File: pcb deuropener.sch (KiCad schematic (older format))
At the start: 34 parts, among them J1 LED 1, J10 Duo LED, J11 Barrel_Jack_Switch, J12 RFID RC522, J13 Solenoid 12V, J14 jumper, J2 Button 2, J3 LED 2, J4 Button 1, J5 Buzzer 12V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

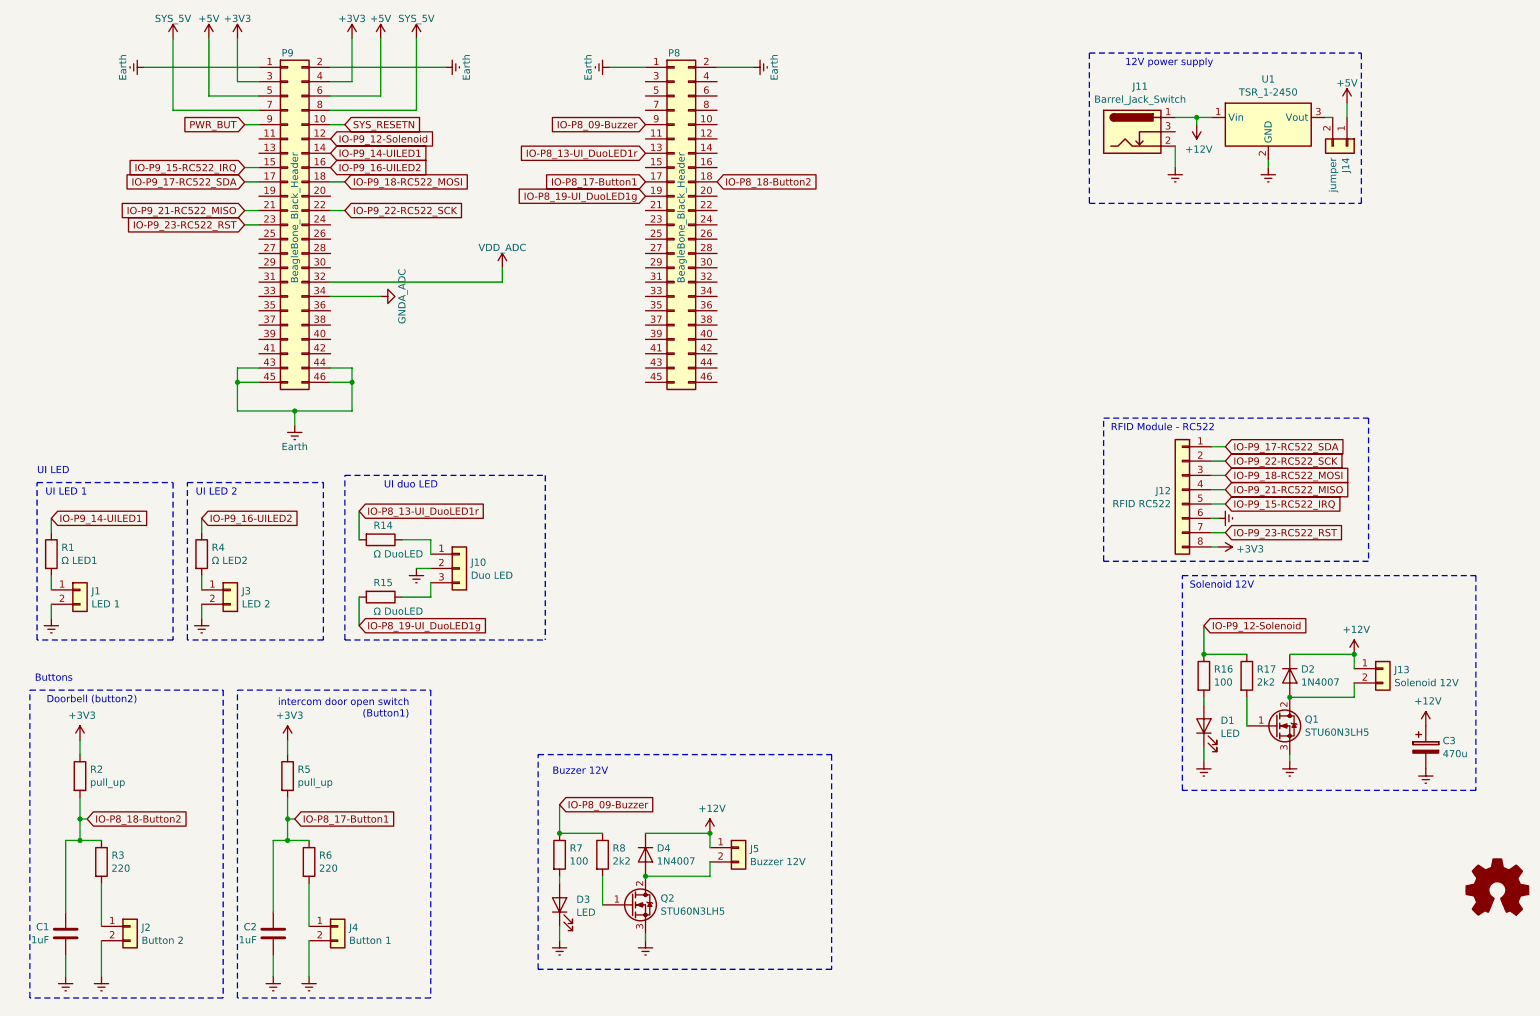
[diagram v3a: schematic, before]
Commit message: Remove a lot of parts and traces
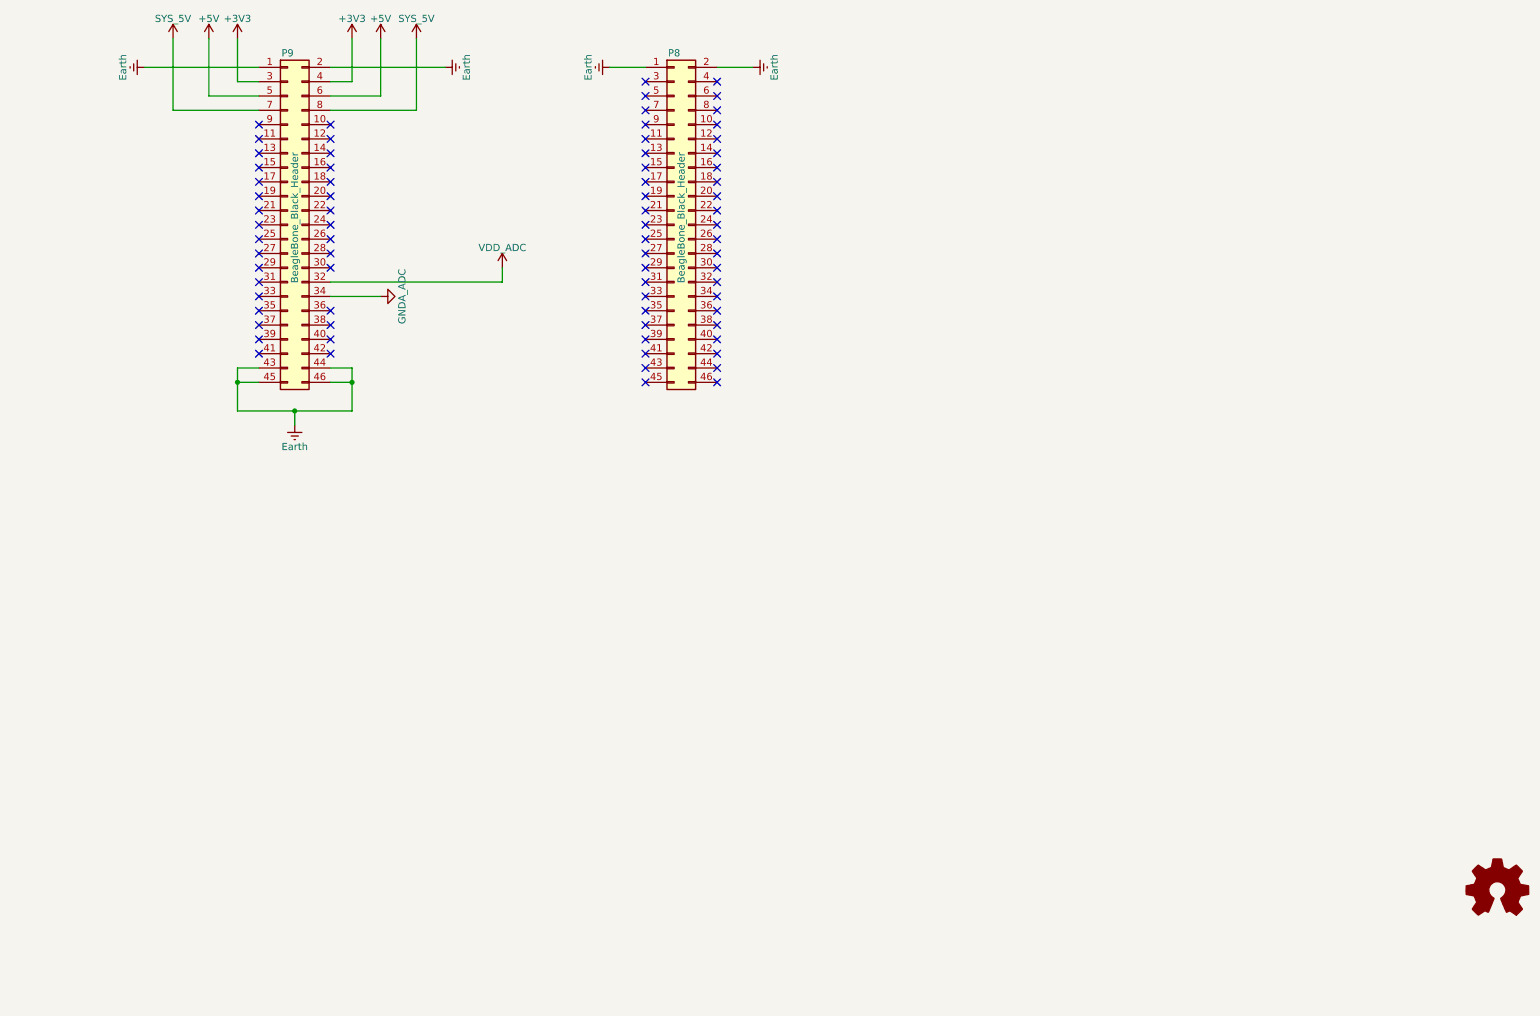
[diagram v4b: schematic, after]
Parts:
- removed C1, C2: 1uF, Capacitor_THT:C_Disc_D7.5mm_W4.4mm_P5.00mm, symbol Device:C
- removed C3: 470u, Capacitor_THT:CP_Radial_D10.0mm_P5.00mm, symbol Device:CP
- removed D1, D3: LED, LED_THT:LED_D5.0mm, symbol Device:LED
- removed D2, D4: 1N4007, Diode_THT:D_DO-41_SOD81_P10.16mm_Horizontal, symbol Diode:1N4007
- removed J1: LED 1, Connector_PinHeader_2.54mm:PinHeader_1x02_P2.54mm_Vertical, symbol Connector_Generic:Conn_01x02
- removed J10: Duo LED, Connector_PinHeader_2.54mm:PinHeader_1x03_P2.54mm_Vertical, symbol Connector_Generic:Conn_01x03
- removed J11: Barrel_Jack_Switch, Connector_BarrelJack:BarrelJack_Horizontal, symbol Connector:Barrel_Jack_Switch
- removed J12: RFID RC522, Connector_PinHeader_2.54mm:PinHeader_1x08_P2.54mm_Vertical, symbol Connector_Generic:Conn_01x08
- removed J13: Solenoid 12V, Connector_PinHeader_2.54mm:PinHeader_1x02_P2.54mm_Vertical, symbol Connector_Generic:Conn_01x02
- removed J14: jumper, Connector_PinHeader_2.54mm:PinHeader_1x02_P2.54mm_Vertical, symbol Connector_Generic:Conn_01x02
- removed J2: Button 2, Connector_PinHeader_2.54mm:PinHeader_1x02_P2.54mm_Vertical, symbol Connector_Generic:Conn_01x02
- removed J3: LED 2, Connector_PinHeader_2.54mm:PinHeader_1x02_P2.54mm_Vertical, symbol Connector_Generic:Conn_01x02
- removed J4: Button 1, Connector_PinHeader_2.54mm:PinHeader_1x02_P2.54mm_Vertical, symbol Connector_Generic:Conn_01x02
- removed J5: Buzzer 12V, Connector_PinHeader_2.54mm:PinHeader_1x02_P2.54mm_Vertical, symbol Connector_Generic:Conn_01x02
- removed Q1, Q2: STU60N3LH5, Package_TO_SOT_THT:SIPAK_Vertical, symbol Device:Q_NMOS_GDS
- removed R1: Ω LED1, Resistor_THT:R_Axial_DIN0207_L6.3mm_D2.5mm_P10.16mm_Horizontal, symbol Device:R
- removed R14, R15: Ω DuoLED, Resistor_THT:R_Axial_DIN0207_L6.3mm_D2.5mm_P10.16mm_Horizontal, symbol Device:R
- removed R16, R7: 100, Resistor_THT:R_Axial_DIN0207_L6.3mm_D2.5mm_P10.16mm_Horizontal, symbol Device:R
- removed R17, R8: 2k2, Resistor_THT:R_Axial_DIN0207_L6.3mm_D2.5mm_P10.16mm_Horizontal, symbol Device:R
- removed R2, R5: pull_up, Resistor_THT:R_Axial_DIN0207_L6.3mm_D2.5mm_P10.16mm_Horizontal, symbol Device:R
- removed R3, R6: 220, Resistor_THT:R_Axial_DIN0207_L6.3mm_D2.5mm_P10.16mm_Horizontal, symbol Device:R
- removed R4: Ω LED2, Resistor_THT:R_Axial_DIN0207_L6.3mm_D2.5mm_P10.16mm_Horizontal, symbol Device:R
- removed U1: TSR_1-2450, Converter_DCDC:Converter_DCDC_TRACO_TSR-1_THT, symbol Regulator_Switching:TSR_1-2450
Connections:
- net IO-P8_09-Buzzer: no longer names the net of P8.9 (Pin_9)
- net IO-P8_13-UI_DuoLED1r: no longer names the net of P8.13 (Pin_13)
- net IO-P8_17-Button1: no longer names the net of P8.17 (Pin_17)
- net IO-P8_18-Button2: no longer names the net of P8.18 (Pin_18)
- net IO-P8_19-UI_DuoLED1g: no longer names the net of P8.19 (Pin_19)
- net IO-P9_12-Solenoid: no longer names the net of P9.12 (Pin_12)
- net IO-P9_14-UILED1: no longer names the net of P9.14 (Pin_14)
- net IO-P9_15-RC522_IRQ: no longer names the net of P9.15 (Pin_15)
- net IO-P9_16-UILED2: no longer names the net of P9.16 (Pin_16)
- net IO-P9_17-RC522_SDA: no longer names the net of P9.17 (Pin_17)
- net IO-P9_18-RC522_MOSI: no longer names the net of P9.18 (Pin_18)
- net IO-P9_21-RC522_MISO: no longer names the net of P9.21 (Pin_21)
- net IO-P9_22-RC522_SCK: no longer names the net of P9.22 (Pin_22)
- net IO-P9_23-RC522_RST: no longer names the net of P9.23 (Pin_23)
- net PWR_BUT: no longer names the net of P9.9 (Pin_9)
- net SYS_RESETN: no longer names the net of P9.10 (Pin_10)
- no-connect marks 0 -> 76
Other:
- note removed: "12V power supply"
- note removed: "Buttons"
- note removed: "Buzzer 12V"
- note removed: "Doorbell (button2)"
- note removed: "RFID Module - RC522"
- note removed: "Solenoid 12V"
- note removed: "UI LED"
- note removed: "UI LED 1"
- note removed: "UI LED 2"
- note removed: "UI duo LED"
- note removed: "intercom door open switch \n(Button1)"
